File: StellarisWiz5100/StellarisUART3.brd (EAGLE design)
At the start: 93 x 84.4 mm, 6 parts

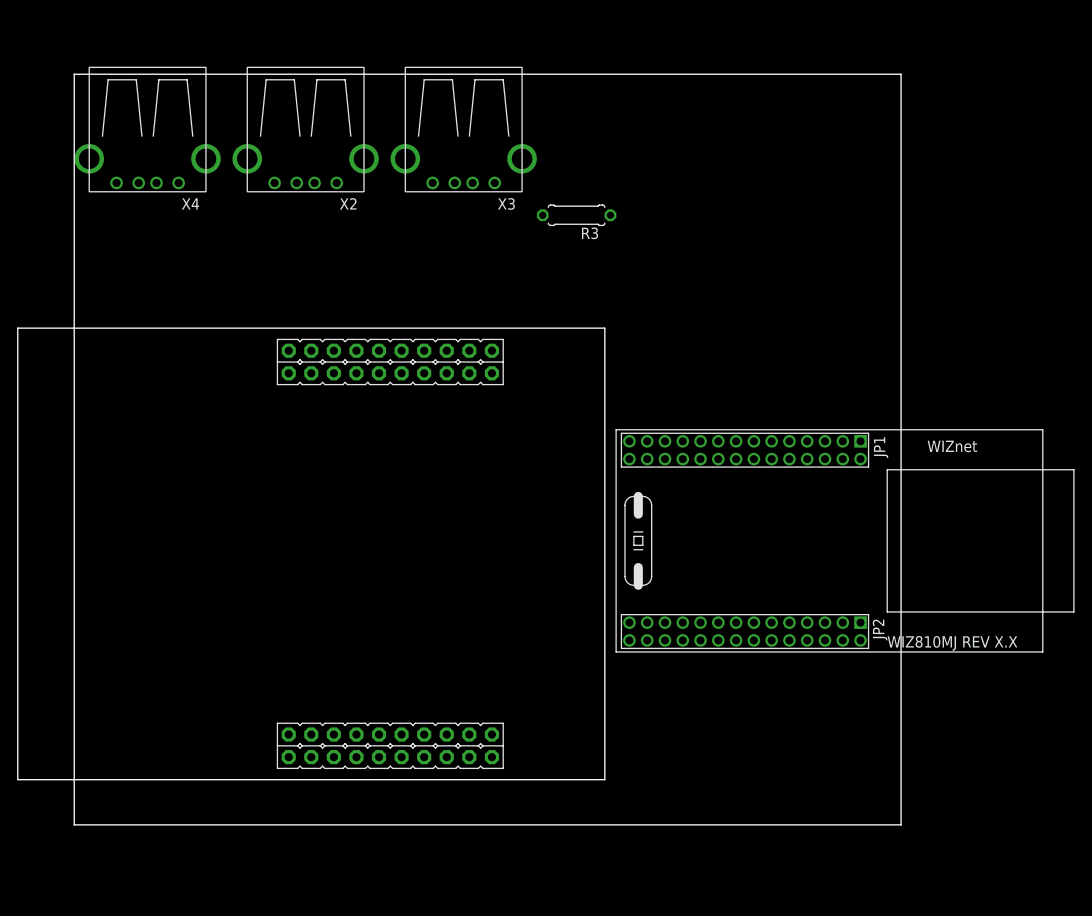
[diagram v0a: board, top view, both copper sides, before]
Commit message: 
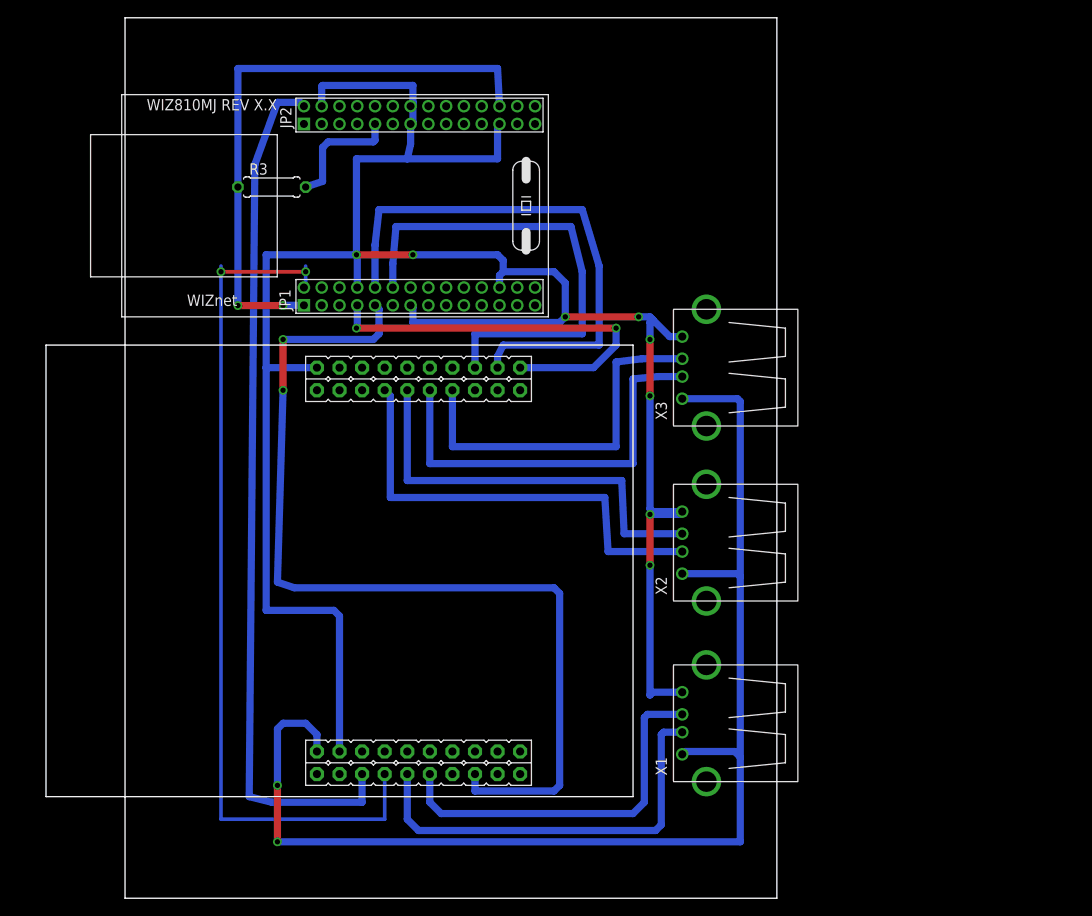
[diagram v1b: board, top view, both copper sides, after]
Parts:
- removed X4: (no value), lieven:USB-A-H
- added X1: (no value), lieven:USB-A-H
- moved X2 62.4 mm to (71.1, 31.8), turned to 180 degrees
- moved X3 36.0 mm to (71.1, 51.4), turned to 180 degrees
- moved R3 34.4 mm to (22.2, 71.8), turned to 0 degrees
- moved U$2 14.8 mm to (53.3, 57.1), turned to 180 degrees
- moved U$1 3.70 mm to (-3.17, 3.17)
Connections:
- removed net N$15: U$1.PE0, X4.D-
- removed net N$16: U$1.PE1, X4.D+
- new net N$2: U$1.PE5, X1.D+
- new net N$4: U$1.PE4, X1.D-
- new net N$5: U$1.PB1, U$2.2
- net +5V: now also X1.VBUS; no longer X4.VBUS
- net GND: now also X1.GND; no longer X4.GND
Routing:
- net GND: track 0.00 -> 254.0 mm, vias 0 -> 8
- net +5V: track 0.00 -> 141.7 mm, vias 0 -> 2
- net N$6: track 0.00 -> 107.2 mm, vias 0 -> 2
- net N$5: track 0.00 -> 97.7 mm, vias 0 -> 2
- net N$1: track 0.00 -> 97.7 mm
- net VCC: track 0.00 -> 67.6 mm, vias 0 -> 2
- net N$9: track 0.00 -> 60.7 mm
- net N$8: track 0.00 -> 54.7 mm
- net N$11: track 0.00 -> 50.9 mm
- net N$4: track 0.00 -> 47.1 mm
- net N$12: track 0.00 -> 46.8 mm
- net N$13: track 0.00 -> 46.2 mm
- net N$3: track 0.00 -> 45.6 mm, vias 0 -> 2
- net N$2: track 0.00 -> 42.3 mm
- net N$14: track 0.00 -> 41.8 mm
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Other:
- board size 93 x 84.4 mm -> 73.3 x 99 mm
